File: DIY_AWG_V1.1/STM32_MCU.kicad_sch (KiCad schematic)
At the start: 28 parts, among them J1 Conn_01x04_Pin, SW1 SW_Push, SW2 SW_Push, U10 STM32G473VETx, U8 USBLC6-2SC6, U9 161N-4BVS11, X1 SX2M8.000B10F20TNN

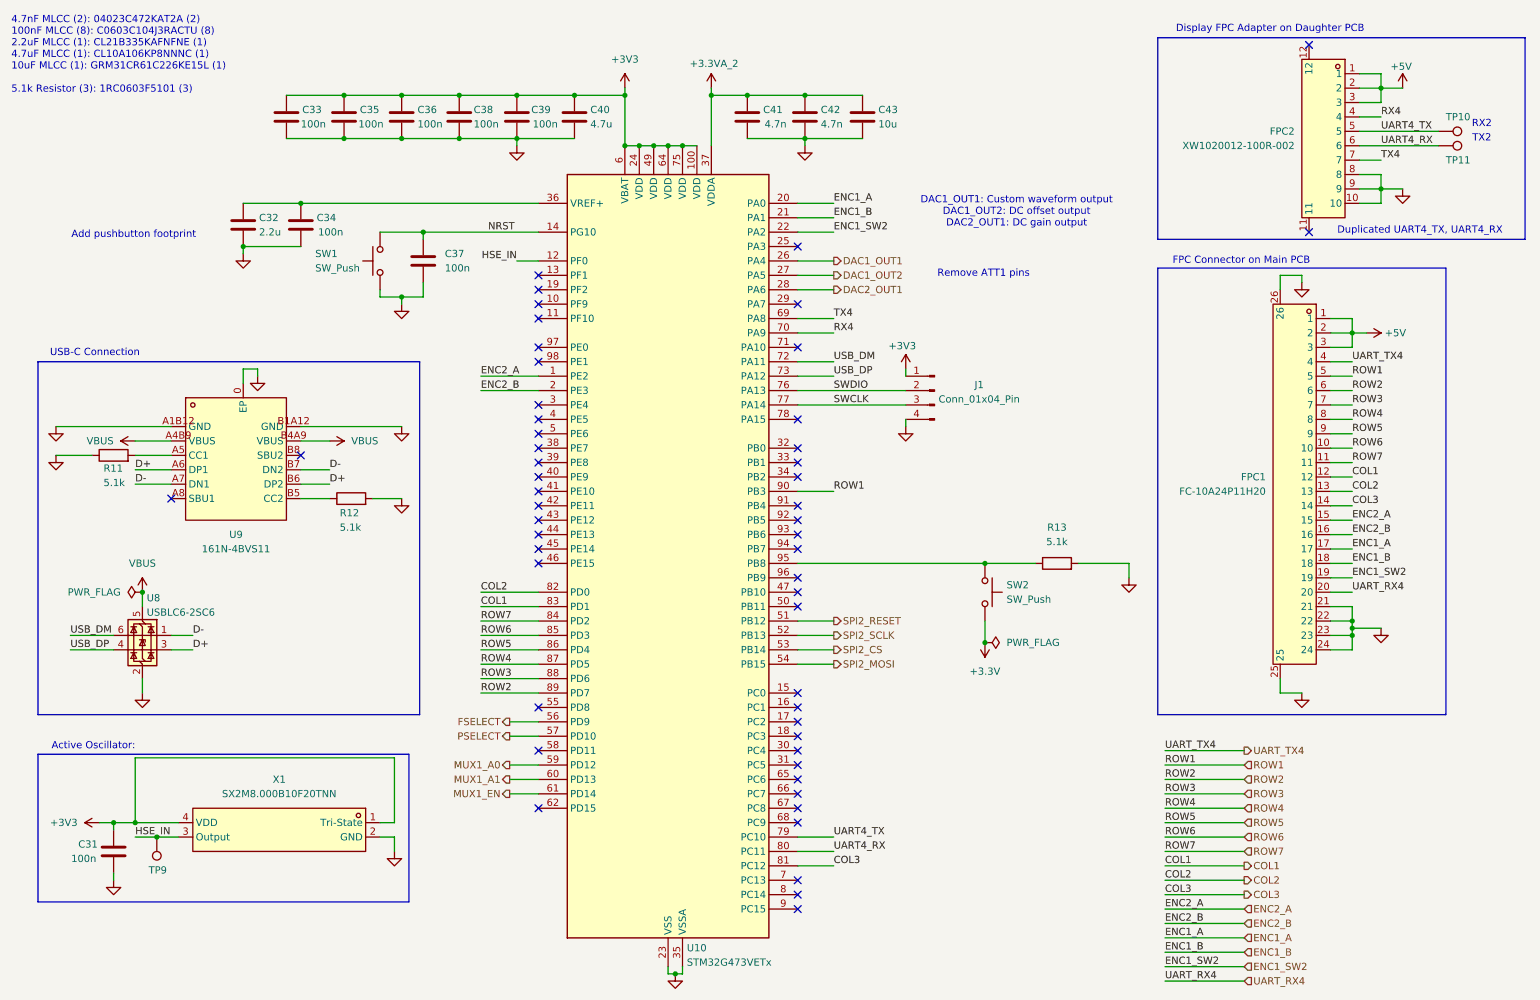
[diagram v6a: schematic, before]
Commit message: Updated component footprints
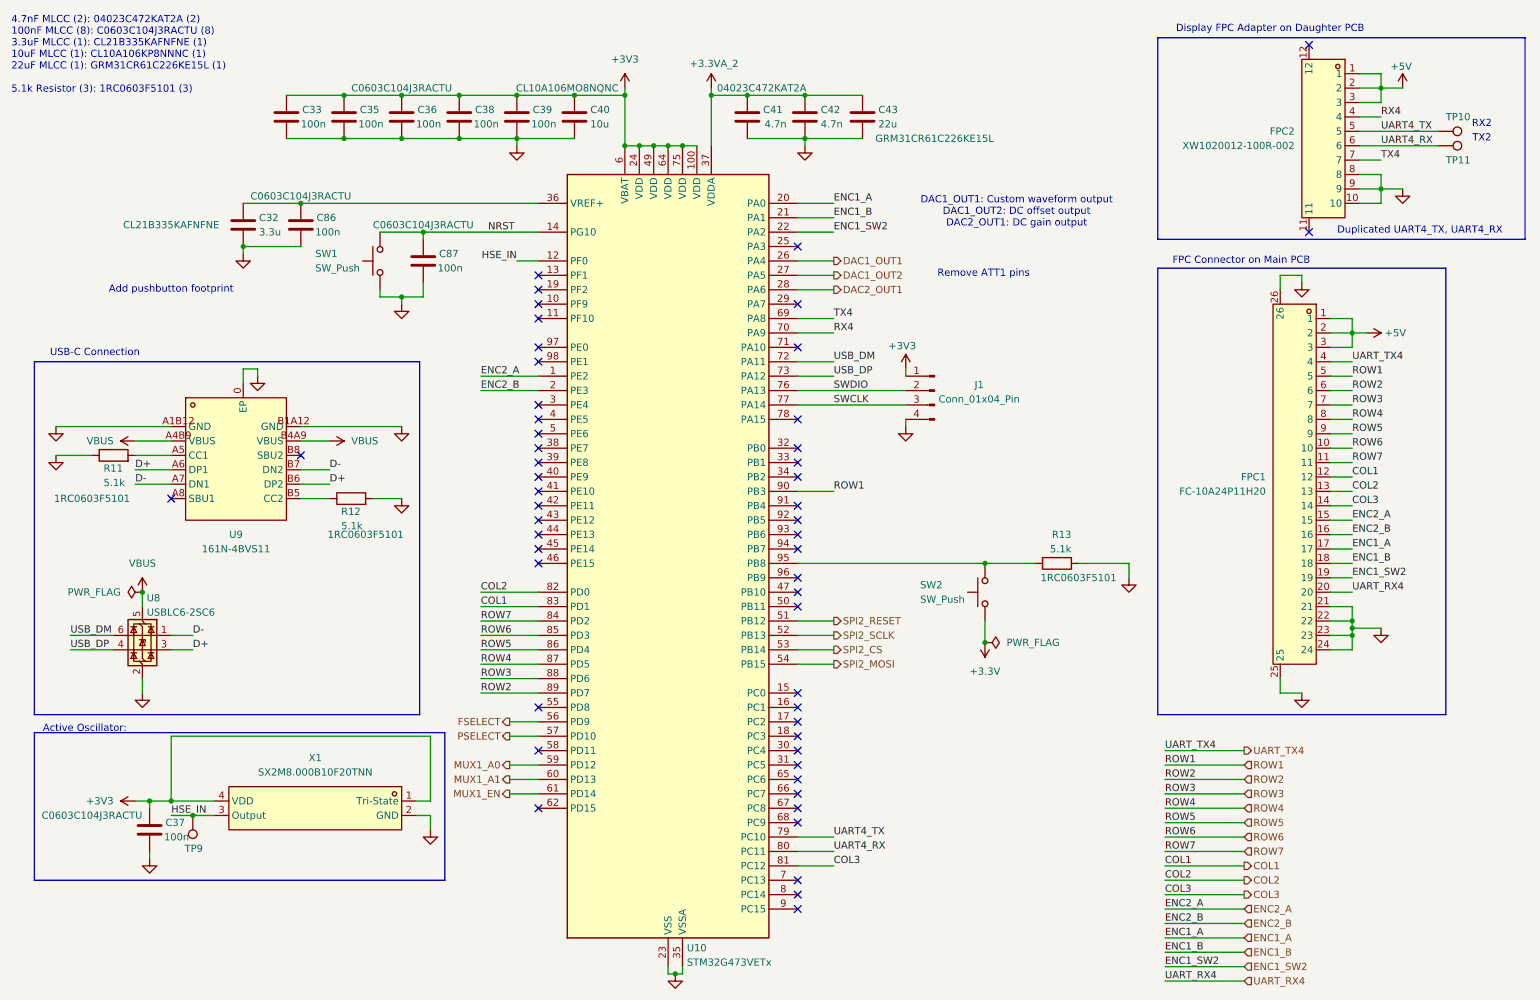
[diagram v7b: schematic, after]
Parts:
- removed C31, C34: 100n, symbol Device:C
- added C86, C87: 100n, Capacitor_SMD:C_0603_1608Metric, symbol Device:C
- C32: value 2.2u -> 3.3u; footprint (none) -> Capacitor_SMD:C_0805_2012Metric; Component Name (none) -> CL21B335KAFNFNE; LCSC ID (none) -> C16194987
- C33, C35, C36, C37, C38, C39: footprint (none) -> Capacitor_SMD:C_0603_1608Metric; Component Name (none) -> C0603C104J3RACTU; LCSC ID (none) -> C2167388
- C40: value 4.7u -> 10u; footprint (none) -> Capacitor_SMD:C_0603_1608Metric; Component Name (none) -> CL10A106MO8NQNC; LCSC ID (none) -> C92487
- C41: footprint (none) -> Capacitor_SMD:C_0402_1005Metric; Component Name (none) -> 04023C472KAT2A; LCSC ID (none) -> C5128374
- C43: value 10u -> 22u; footprint (none) -> Capacitor_SMD:C_1206_3216Metric; Component Name (none) -> GRM31CR61C226KE15L; LCSC ID (none) -> C77088
- R11, R12, R13: footprint (none) -> Resistor_SMD:R_0603_1608Metric; Component Name (none) -> 1RC0603F5101; LCSC ID (none) -> C53224208
- SW1, SW2: footprint (none) -> easyeda2kicad:SW-SMD_L6.1-W3.5-LS8.6; Component Name (none) -> LCK-TA003H43-2WL; LCSC ID (none) -> C51978298
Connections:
- net +3.3V: now also SW2.1; no longer SW2.2
- net +3V3: now also C37.1
- net GND: now also C86.2, C87.2
- net NRST: now also C87.1; no longer C37.1
- net at R13.1, U10.95 (PB8): now also SW2.2; no longer SW2.1
- net at C32.1, U10.36 (VREF+): now also C86.1
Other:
- note added: "4.7nF MLCC (2): 04023C472KAT2A (2) 100nF MLCC (8): C0603C104J3RACTU (8) 3.3uF MLCC (1): CL21B335KAFNFNE (1) 10uF MLCC (1): CL10A106KP8NNNC (1) 22uF MLCC (1): GRM31CR61C226KE15L (1) 5.1k Resistor (3): 1RC0603F5101 (3)"
- note removed: "4.7nF MLCC (2): 04023C472KAT2A (2) 100nF MLCC (8): C0603C104J3RACTU (8) 2.2uF MLCC (1): CL21B335KAFNFNE (1) 4.7uF MLCC (1): CL10A106KP8NNNC (1) 10uF MLCC (1): GRM31CR61C226KE15L (1) 5.1k Resistor (3): 1RC0603F5101 (3)"
- moved on the sheet: TP9, X1

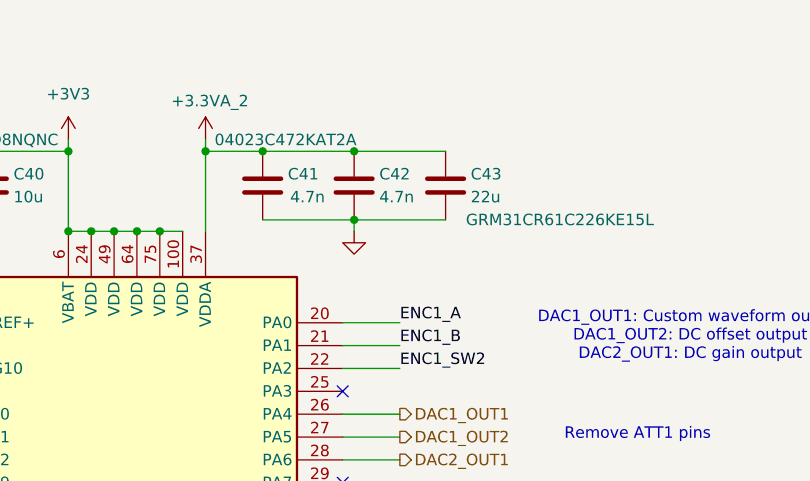
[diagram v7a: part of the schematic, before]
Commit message: Updated schematic footprints
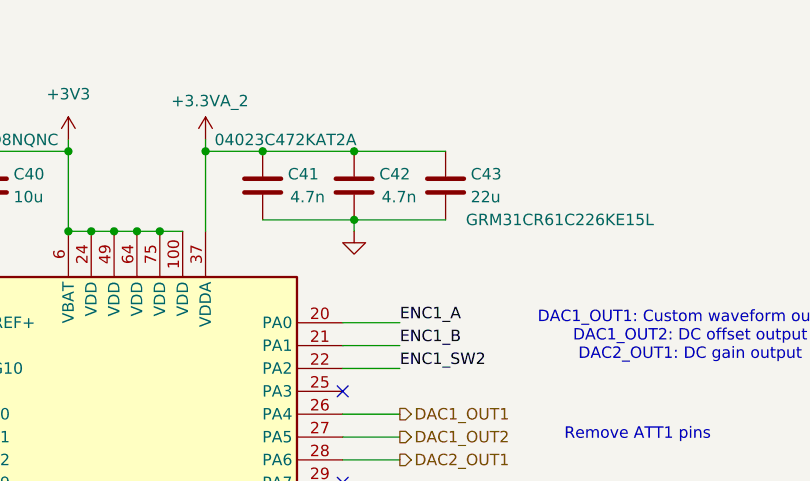
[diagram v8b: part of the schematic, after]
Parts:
- C42: Component Name (none) -> 04023C472KAT2A; LCSC ID (none) -> C5128374
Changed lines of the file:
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@@
 	)
 	(junction
-		(at 156.21 27.94)
-		(diameter 0)
-		(color 0 0 0 0)
-	)
-	(junction
 		(at 85.09 27.94)
 		(diameter 0)
@@
 	)
 	(junction
+		(at 156.21 27.94)
+		(diameter 0)
+		(color 0 0 0 0)
+	)
+	(junction
 		(at 95.25 27.94)
 		(diameter 0)
@@
 	(wire
 		(pts
-			(xy 156.21 27.94) (xy 166.37 27.94)
+			(xy 146.05 27.94) (xy 156.21 27.94)
 		)
 		(stroke
@@
 	(wire
 		(pts
-			(xy 146.05 27.94) (xy 156.21 27.94)
-		)
-		(stroke
-			(width 0)
-			(type default)
-		)
-	)
-	(wire
-		(pts
 			(xy 213.36 110.49) (xy 213.36 113.03)
 		)
@@
 	(wire
 		(pts
+			(xy 156.21 27.94) (xy 166.37 27.94)
+		)
+		(stroke
+			(width 0)
+			(type default)
+		)
+	)
+	(wire
+		(pts
 			(xy 67.31 46.99) (xy 109.22 46.99)
 		)
@@
 	)
 	(symbol
-		(lib_id "Device:C")
-		(at 156.21 31.75 0)
-		(unit 1)
-		(body_style 1)
-		(exclude_from_sim no)
-		(in_bom yes)
-		(on_board yes)
-		(in_pos_files yes)
-		(dnp no)
-		(property "Reference" "C42"
-			(at 159.004 30.48 0)
-			(show_name no)
-			(do_not_autoplace no)
-			(effects
-				(font
-					(size 1.27 1.27)
-				)
-				(justify left)
-			)
-		)
-		(property "Value" "4.7n"
-			(at 159.004 33.02 0)
-			(show_name no)
-			(do_not_autoplace no)
-			(effects
-				(font
-					(size 1.27 1.27)
-				)
-				(justify left)
-			)
-		)
-		(property "Footprint" ""
-			(at 157.1752 35.56 0)
-			(hide yes)
-			(show_name no)
-			(do_not_autoplace no)
-			(effects
-				(font
-					(size 1.27 1.27)
-				)
-			)
-		)
-		(property "Datasheet" ""
-			(at 156.21 31.75 0)
-			(hide yes)
-			(show_name no)
-			(do_not_autoplace no)
-			(effects
-				(font
-					(size 1.27 1.27)
-				)
-			)
-		)
-		(property "Description" "Unpolarized capacitor"
-			(at 156.21 31.75 0)
-			(hide yes)
-			(show_name no)
-			(do_not_autoplace no)
-			(effects
-				(font
-					(size 1.27 1.27)
-				)
-			)
-		)
-		(pin "2"
-		)
-		(pin "1"
-		)
-		(instances
-			(project "DIY_AWG_V1.1"
-				(path "/508078af-d961-4af3-840e-a064a9f8d5bc/aaba8d51-2713-41de-9761-99ebb3cee83e"
-					(reference "C42")
-					(unit 1)
-				)
-			)
-		)
-	)
-	(symbol
 		(lib_id "power:PWR_FLAG")
 		(at 187.96 124.46 270)
@@
 					(unit 1)
 				)
+			)
+		)
+	)
+	(symbol
+		(lib_id "Device:C")
+		(at 156.21 31.75 0)
+		(unit 1)
+		(body_style 1)
+		(exclude_from_sim no)
+		(in_bom yes)
+		(on_board yes)
+		(in_pos_files yes)
+		(dnp no)
+		(property "Reference" "C42"
+			(at 159.004 30.48 0)
+			(show_name no)
+			(do_not_autoplace no)
+			(effects
+				(font
+					(size 1.27 1.27)
+				)
+				(justify left)
+			)
+		)
+		(property "Value" "4.7n"
+			(at 159.258 33.02 0)
+			(show_name no)
+			(do_not_autoplace no)
+			(effects
+				(font
+					(size 1.27 1.27)
+				)
+				(justify left)
+			)
+		)
+		(property "Footprint" ""
+			(at 157.1752 35.56 0)
+			(hide yes)
+			(show_name no)
+			(do_not_autoplace no)
+			(effects
+				(font
+					(size 1.27 1.27)
+				)
+			)
+		)
+		(property "Datasheet" "https://datasheets.kyocera-avx.com/KGM_X7R.pdf"
+			(at 156.21 31.75 0)
+			(hide yes)
+			(show_name no)
+			(do_not_autoplace no)
+			(effects
+				(font
+					(size 1.27 1.27)
+				)
+			)
+		)
+		(property "Description" "Unpolarized capacitor"
+			(at 156.21 31.75 0)
+			(hide yes)
+			(show_name no)
+			(do_not_autoplace no)
+			(effects
+				(font
+					(size 1.27 1.27)
+				)
+			)
+		)
+		(property "Component Name" "04023C472KAT2A"
+			(at 158.75 26.67 0)
+			(hide yes)
+			(show_name no)
+			(do_not_autoplace no)
+			(effects
+				(font
+					(size 1.27 1.27)
+				)
+			)
+		)
+		(property "LCSC ID" "C5128374"
+			(at 156.21 31.75 0)
+			(hide yes)
+			(show_name no)
+			(do_not_autoplace no)
+			(effects
+				(font
+					(size 1.27 1.27)
+				)
+			)
+		)
+		(pin "2"
+		)
+		(pin "1"
+		)
+		(instances
+			(project "DIY_AWG_V1.1"
+				(path "/508078af-d961-4af3-840e-a064a9f8d5bc/aaba8d51-2713-41de-9761-99ebb3cee83e"
+					(reference "C42")
+					(unit 1)
+				)
